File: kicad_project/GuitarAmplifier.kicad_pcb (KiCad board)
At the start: 4 copper layers, 158.5 x 57 mm, 45 parts, among them J1 NMJ6HCD2, J2 Screw_Terminal_01x02, J3 Screw_Terminal_01x02, J4 Terminal_01x03, U1 TL072CP, U2 TL072CP, U3 LM386

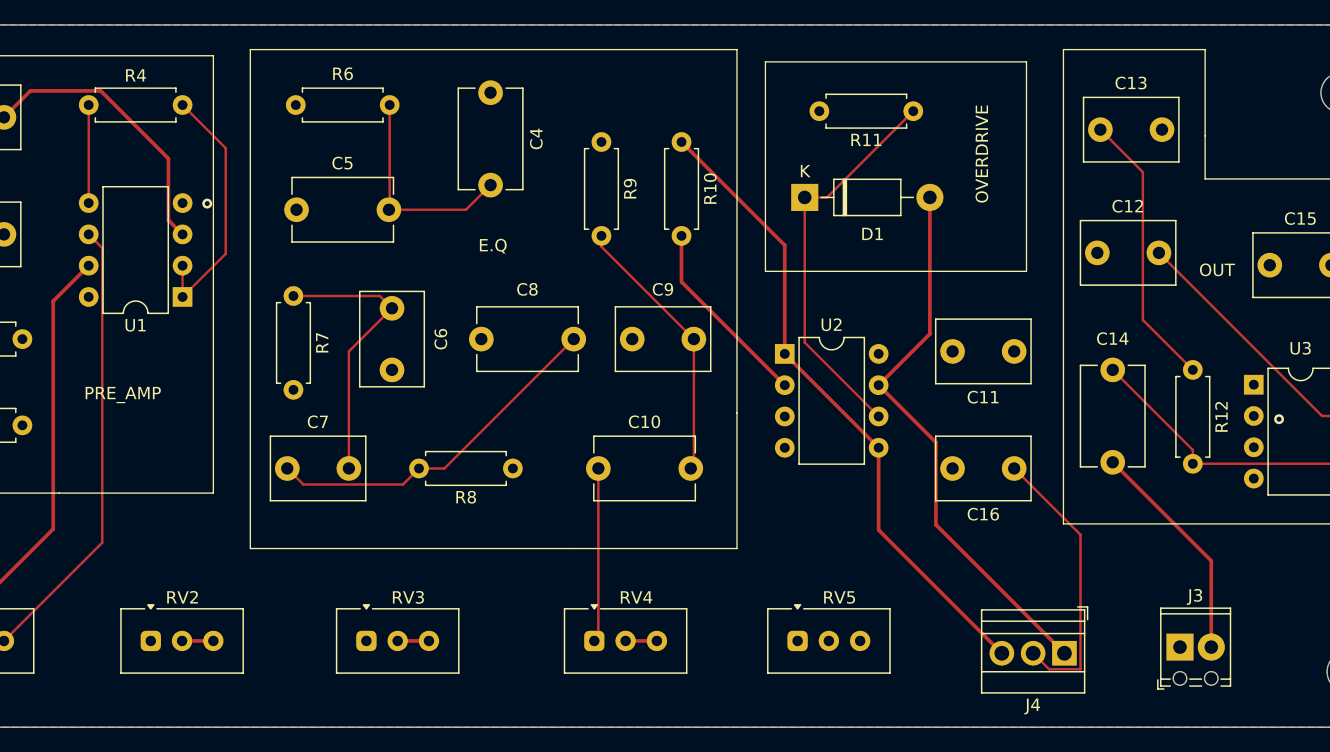
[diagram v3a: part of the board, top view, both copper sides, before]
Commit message: Agregando el enrutamiento final y una reconfiguración de la placa
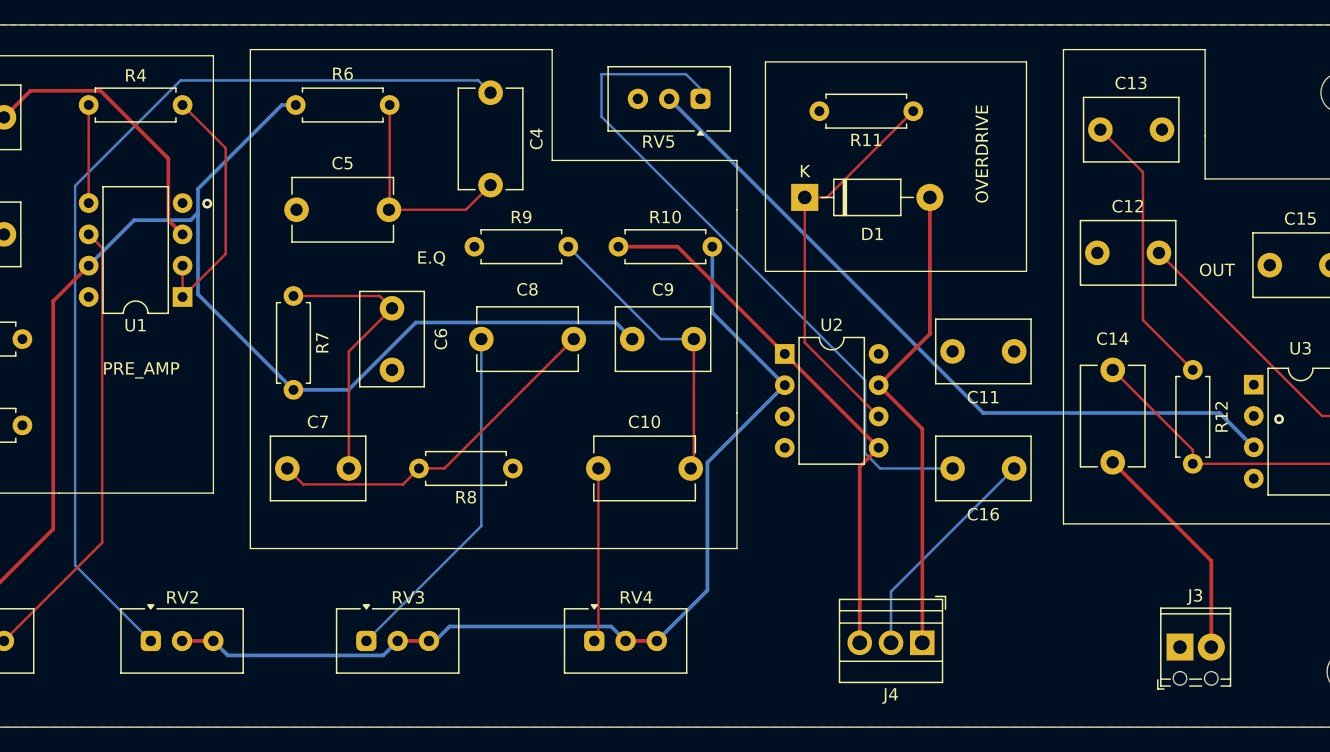
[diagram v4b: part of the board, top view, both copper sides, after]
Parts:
- moved RV5 44.7 mm to (201.5, 118.5), turned to 180 degrees
- moved R9 13.4 mm to (183.2, 130.5), turned to 0 degrees
- moved J4 11.6 mm to (219.5, 162.7)
- moved R10 9.92 mm to (194.9, 130.5), turned to 0 degrees
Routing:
- net Net-(C4-Pad1): track 0.00 -> 77.2 mm
- net /OUT_PreAmp: track 35.4 -> 106.7 mm
- net Net-(U3-+): track 0.00 -> 59.5 mm
- net Net-(C16-Pad2): track 0.00 -> 56.6 mm
- net /OUT_Eq: track 23.2 -> 79.2 mm
- net Net-(C8-Pad1): track 0.00 -> 28.4 mm
- net /OUT_Clean: track 52.3 -> 44.3 mm
- net /OUT_OverD: track 45.0 -> 39.3 mm
- net Net-(J4-Pin_2): track 22.9 -> 18.3 mm
- net Net-(C10-Pad2): track 22.1 -> 23.9 mm

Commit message: Terminando de rellenar la capa inferior y ajustando las huellas de los conectores
Signed-off-by: RoMadrigal <rmadrigalmontes@gmail.com>
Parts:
- J2, J3: footprint TerminalBlock_Phoenix:TerminalBlock_Phoenix_MPT-0,5-2-2.54_1x02_P2.54mm_Horizontal -> TerminalBlock:TerminalBlock_bornier-2_P5.08mm
- J4: footprint TerminalBlock:TerminalBlock_Xinya_XY308-2.54-3P_1x03_P2.54mm_Horizontal -> TerminalBlock:TerminalBlock_bornier-3_P5.08mm
- moved J4 10.8 mm to (230.3, 162.8)
- moved J3 1.08 mm to (239.5, 162.5)
- moved J2 0.85 mm to (118.8, 122.5)
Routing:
- net /OUT_OverD: track 39.3 -> 43.9 mm
- net Net-(J4-Pin_2): track 18.3 -> 15.0 mm
- net /OUT_Clean: track 44.3 -> 45.5 mm
- added copper zone on B.Cu, net GND

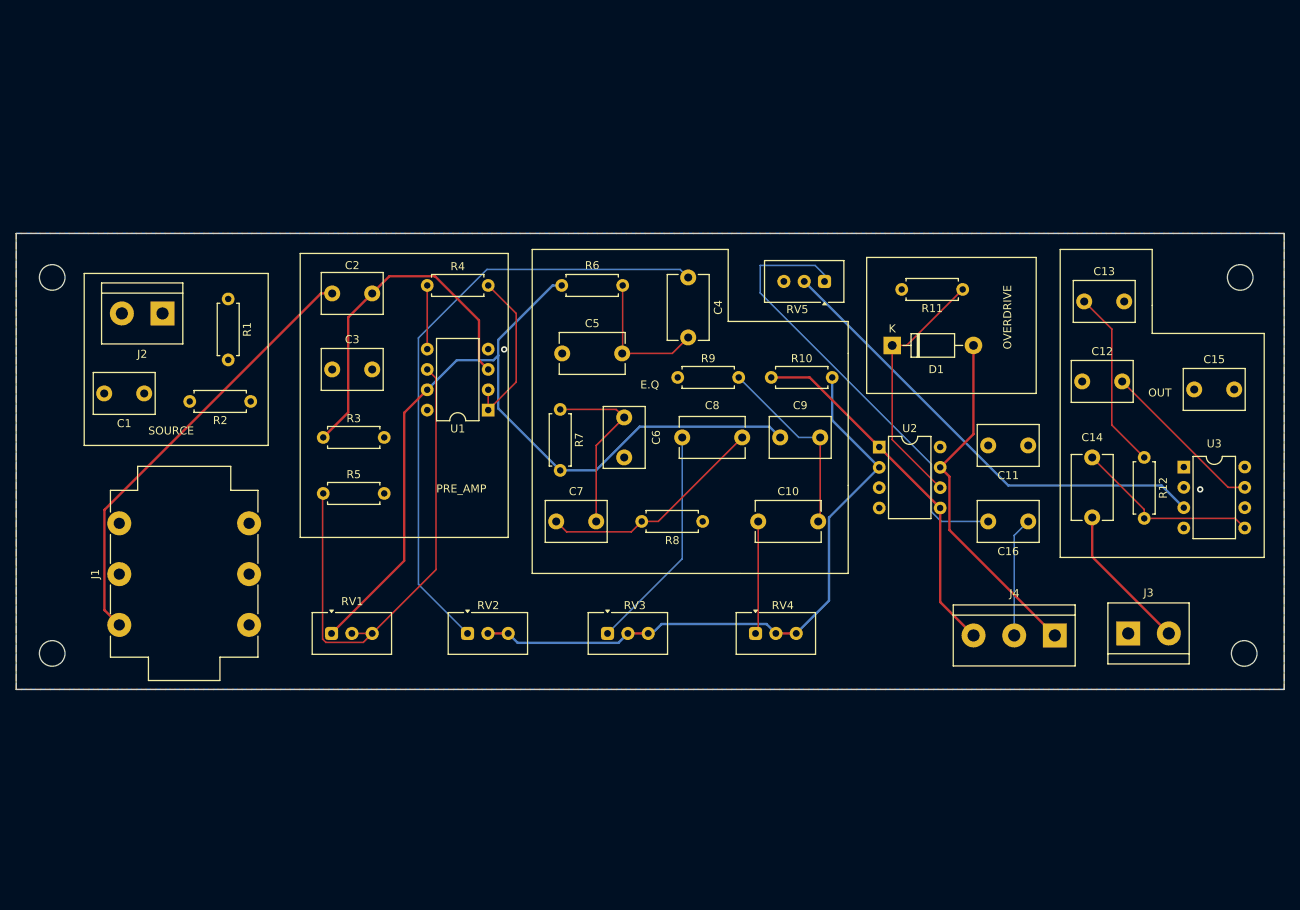
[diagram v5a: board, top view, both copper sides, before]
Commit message: Agregando detalles finales en la serigrafia de la PCB
Signed-off-by: RoMadrigal <rmadrigalmontes@gmail.com>
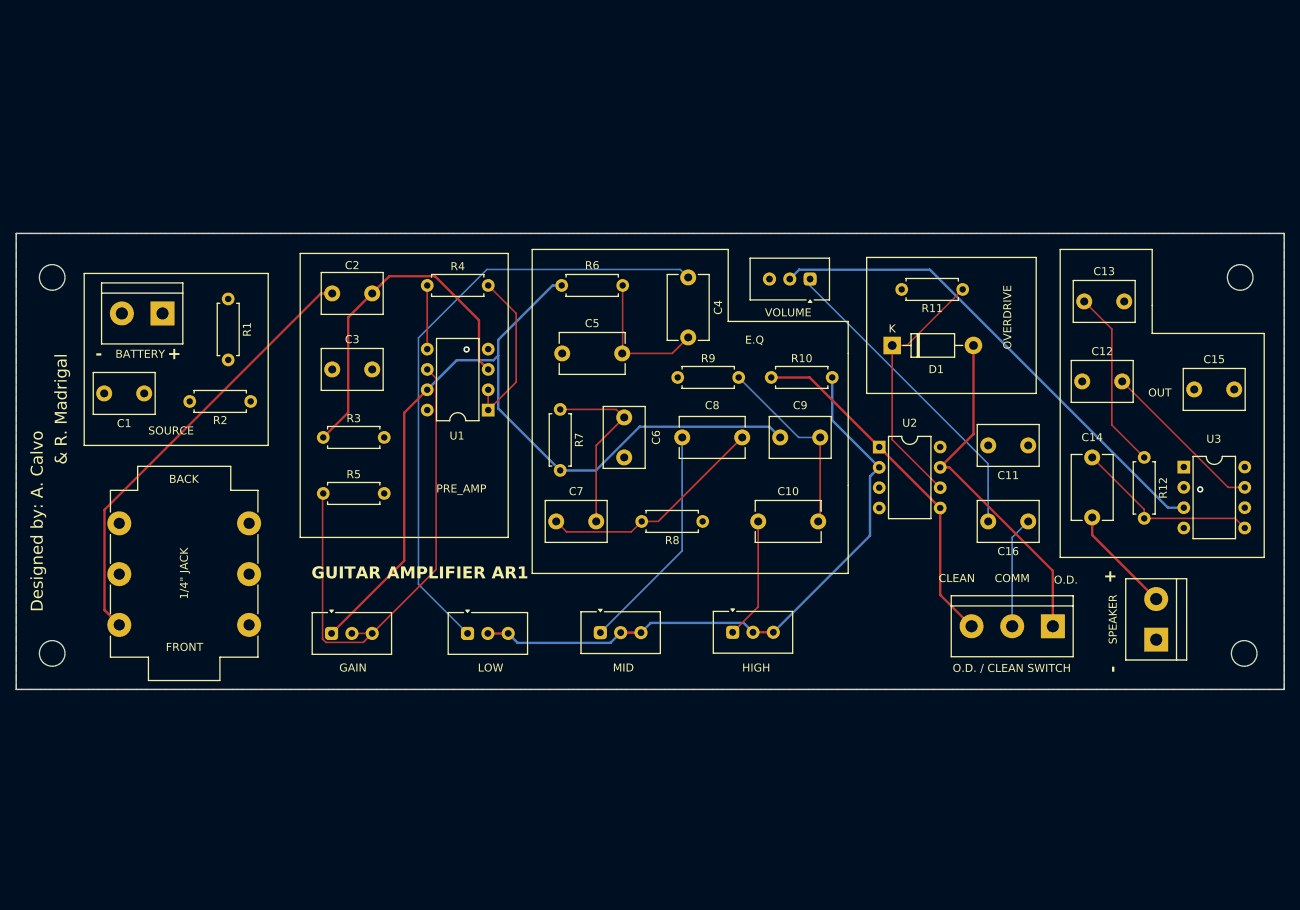
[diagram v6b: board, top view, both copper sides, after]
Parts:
- 1/4" JACK: renamed from J1
- O.D. / CLEAN SWITCH: renamed from J4
- moved SPEAKER 3.59 mm to (243.0, 163.3), turned to 90 degrees
- moved HIGH 2.86 mm to (190.1, 162.4)
- moved VOLUME 1.82 mm to (199.7, 118.2)
- moved O.D. / CLEAN SWITCH 1.18 mm to (230.1, 161.6)
- moved MID 0.91 mm to (173.5, 162.4)
- renumbered J2 to BATTERY, RV1 to GAIN, RV4 to HIGH, RV2 to LOW, RV3 to MID, J3 to SPEAKER, RV5 to VOLUME
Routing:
- net Net-(C16-Pad2): track 56.6 -> 39.5 mm
- net /System_Out: track 18.5 -> 13.5 mm
- net Net-(U3-+): track 59.5 -> 62.1 mm
- net /OUT_Eq: track 79.2 -> 77.9 mm
- net /OUT_Clean: track 45.5 -> 44.3 mm
- net Net-(J4-Pin_2): track 15.0 -> 13.9 mm
- net Net-(C10-Pad1): track 14.1 -> 15.2 mm
- net /OUT_OverD: track 43.9 -> 43.3 mm
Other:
- board text added: "& R. Madrigal"
- board text added: "+"
- board text added: "-"
- board text added: "BACK"
- board text added: "CLEAN"
- board text added: "COMM"
- board text added: "Designed by: A. Calvo"
- board text added: "FRONT"
- board text added: "GUITAR AMPLIFIER AR1"
- board text added: "O.D."

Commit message: Reasignando huella de los potenciometros
Signed-off-by: RoMadrigal <rmadrigalmontes@gmail.com>
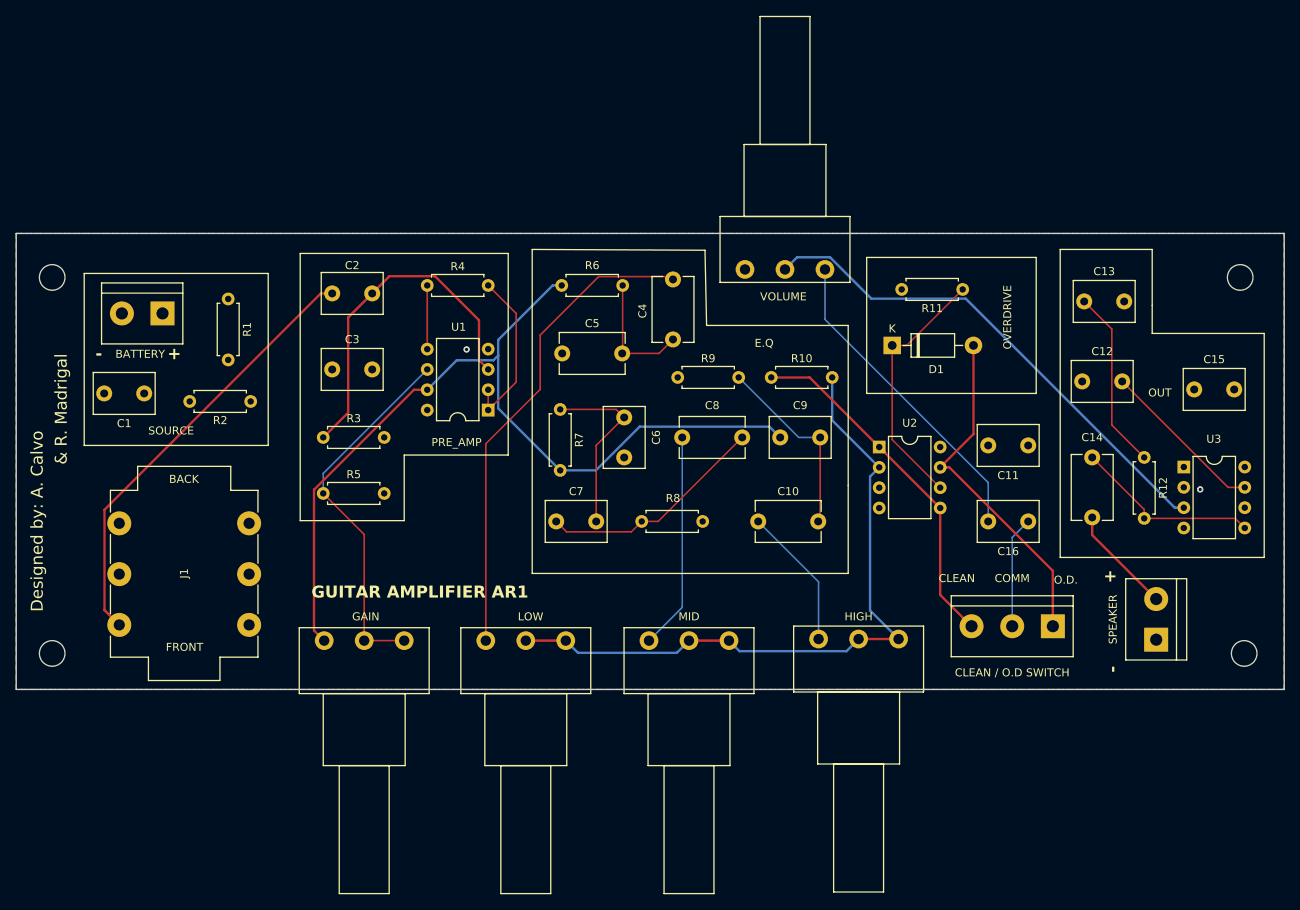
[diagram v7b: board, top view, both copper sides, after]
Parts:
- CLEAN / O.D SWITCH: renamed from O.D. / CLEAN SWITCH
- GAIN, HIGH, LOW, MID, VOLUME: footprint Potentiometer_THT:Potentiometer_Vishay_T93XA_Horizontal -> Potentiometer_THT:Potentiometer_Piher_PC-16_Single_Horizontal
- J1: renamed from 1/4" JACK
- moved HIGH 10.8 mm to (200.8, 163.2), turned to -90 degrees
- moved MID 6.16 mm to (179.6, 163.4), turned to -90 degrees
- moved LOW 2.45 mm to (159.2, 163.4), turned to -90 degrees
- moved VOLUME 2.21 mm to (201.6, 117.0), turned to 90 degrees
- moved C4 1.92 mm to (182.6, 118.2)
- moved GAIN 1.29 mm to (139.0, 163.4), turned to -90 degrees
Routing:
- net Net-(U1-2IN-): track 64.4 -> 46.5 mm
- net Net-(C4-Pad1): track 77.2 -> 60.8 mm
- net /OUT_Eq: track 77.9 -> 86.1 mm
- net /OUT_PreAmp: track 106.7 -> 110.0 mm
- net Net-(C10-Pad1): track 15.2 -> 17.8 mm
- net Net-(C4-Pad2): track 17.6 -> 15.6 mm
- net Net-(C8-Pad1): track 28.6 -> 27.1 mm
- net Net-(U3-+): track 62.1 -> 63.4 mm

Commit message: Agregando logotipos y verificando la configuracion final
Signed-off-by: RoMadrigal <rmadrigalmontes@gmail.com>
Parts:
- added G***: LOGO, PCBWayLogo:PCBWayLogo3, F.Cu at (151.0, 154.4)
- added G***: LOGO, EIELogo:EIELogo3, F.Cu at (155.0, 145.2)
- moved VOLUME 1.40 mm to (201.6, 118.4)
